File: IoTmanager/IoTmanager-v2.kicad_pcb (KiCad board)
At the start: 2 copper layers, 50 x 70.7 mm, 65 parts, among them J2 Conn_01x12_Pin, J3 Conn_01x12_Pin, J4-flash1 flash, J5 reset, K3 ZC32F-012-HS3-copy, K5 ZC32F-012-HS3-copy, K6 ZC32F-012-HS3-copy, K7 ZC32F-012-HS3-copy, Q1-pnp1 MMBT5401, Q10-pnp1 MMBT5401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

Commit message: update
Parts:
- removed U4: Mini360, module-custom-for-esp8266:Mini360_step-down
- added R12-10k2: R-1k, Resistor_SMD:R_0805_2012Metric, B.Cu at (107.7, 63.4)
- added R12-10k3: R-1k, Resistor_SMD:R_0805_2012Metric, B.Cu at (107.7, 66.3)
- added U3: DHT11, Sensor:Aosong_DHT11_5.5x12.0_P2.54mm, F.Cu at (122.6, 127.3)
- moved U5 52.1 mm to (127.0, 109.0), turned to 180 degrees
- moved R21 51.9 mm to (114.0, 126.0), turned to 0 degrees
- moved U3-tsop23 51.5 mm to (121.2, 85.9), turned to 90 degrees
- moved R25 51.3 mm to (82.8, 125.5), turned to 180 degrees
- moved Q10-pnp1 47.3 mm to (82.7, 122.8), turned to 0 degrees
- moved D1 47.2 mm to (122.2, 89.2), turned to -90 degrees
- moved Q5 46.5 mm to (113.7, 122.8), turned to 0 degrees
- moved R26 43.3 mm to (82.8, 120.0), turned to 180 degrees
- moved K3 43.0 mm to (119.0, 111.6), turned to -90 degrees
- moved R22 42.9 mm to (113.9, 120.1), turned to 0 degrees
- moved R4 42.6 mm to (103.7, 125.8), turned to 0 degrees
- moved R23 42.4 mm to (92.9, 125.6), turned to 0 degrees
- moved J2 41.8 mm to (80.0, 130.7), turned to 180 degrees
- moved D6 39.7 mm to (122.4, 112.4), turned to -90 degrees
- moved Q11-npn1 39.7 mm to (82.7, 117.1), turned to 0 degrees
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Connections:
- J2 pad 9: /d0 -> unconnected-(J2-Pin_9-Pad9)
- Jumper-d5 pad 1: /d5 -> Net-(IRLR2-G)
- Jumper-d6 pad 1: /d6 -> Net-(IRLR1-G)
- Jumper-d7 pad 1: /d7 -> Net-(IRLR3-G)
- U2 pad 19: /d2 -> Net-(U2-GPIO4)
- U2 pad 20: /d1 -> Net-(U2-GPIO5)
- U3-tsop23 pad 1: /d5 -> /d1
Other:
- board size 50 x 70.7 mm -> 48 x 80 mm

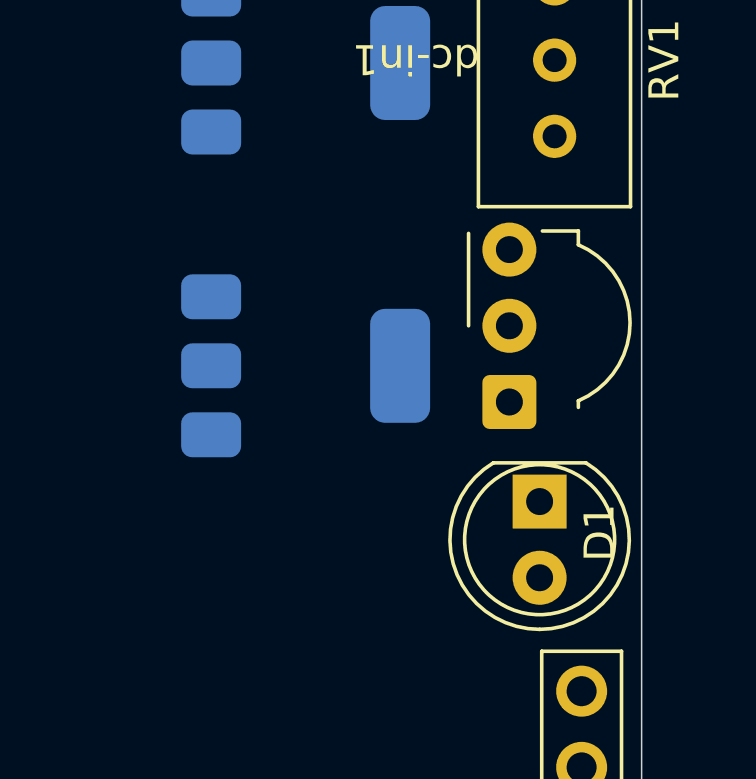
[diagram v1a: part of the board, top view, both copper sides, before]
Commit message: Update IoTmanager schematic and libraries
- Changed paper size from A3 to A2 in IoTmanager schematic.
- Added MMDT4413-7-F symbol and footprint to the schematic and libraries.
- Updated various component properties including reference, value, and footprint.
- Adjusted component placements and added new power symbols for +3.3V and GNDPWR.
- Modified existing project files in Proteous tests, including autosaved versions.
- Updated fp-info-cache with new component details.
- Created new KiCAD symbol and footprint files for MMDT4413-7-F.
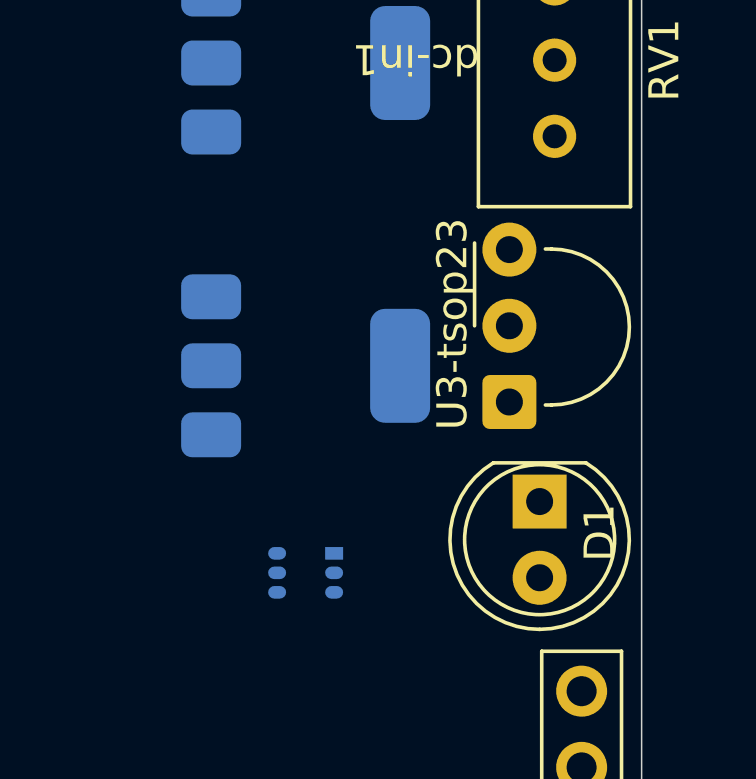
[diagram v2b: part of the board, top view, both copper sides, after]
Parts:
- added U8: MMDT4413-7-F, module-custom-for-esp8266:SOT-363_DIO, B.Cu at (114.4, 91.6)
- U3-tsop23: footprint OptoDevice:Vishay_MOLD-3Pin -> module-custom-for-esp8266:Vishay_MINIMOLD-3Pin_GND_correct
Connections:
- Q5 pad 1: Net-(Q5-B) -> unconnected-(Q5-B-Pad1)
- R21 pad 1: Net-(Q5-B) -> Net-(U8-B2)

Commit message: auto update from EPAM computer
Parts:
- added C3: C_Small, Capacitor_SMD:C_0805_2012Metric_Pad1.18x1.45mm_HandSolder, B.Cu at (117.0, 79.7)
- added R11: R-100, Resistor_SMD:R_0805_2012Metric, B.Cu at (116.5, 90.2)
- moved U8 3.37 mm to (114.0, 94.9)
- moved R7 0.40 mm to (119.5, 120.8)
- moved U3 0.13 mm to (122.7, 127.2)
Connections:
- R16 pad 2: /d8 -> /d2
- U3-tsop23 pad 1: /d1 -> Net-(U3-tsop23-OUT)

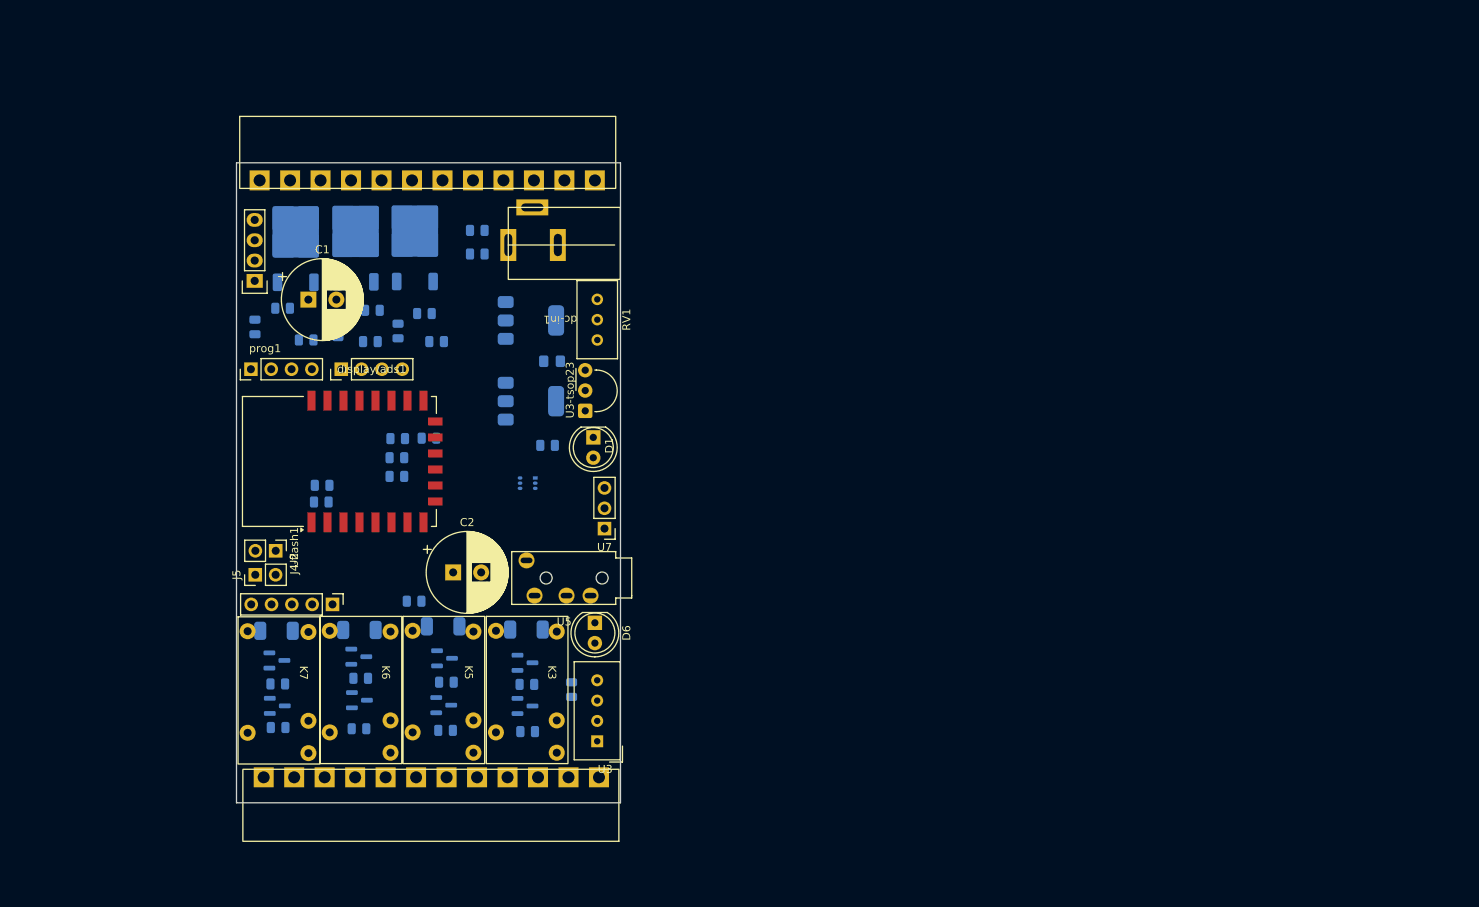
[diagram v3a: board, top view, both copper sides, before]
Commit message: Update fp-info-cache with new audio module and relay specifications
- Updated the ID for the Audio_Module entry.
- Added new relay module (RELAY_SRD-05VDC-SL-C) with specifications.
- Ensured proper formatting and consistency in the module entries.
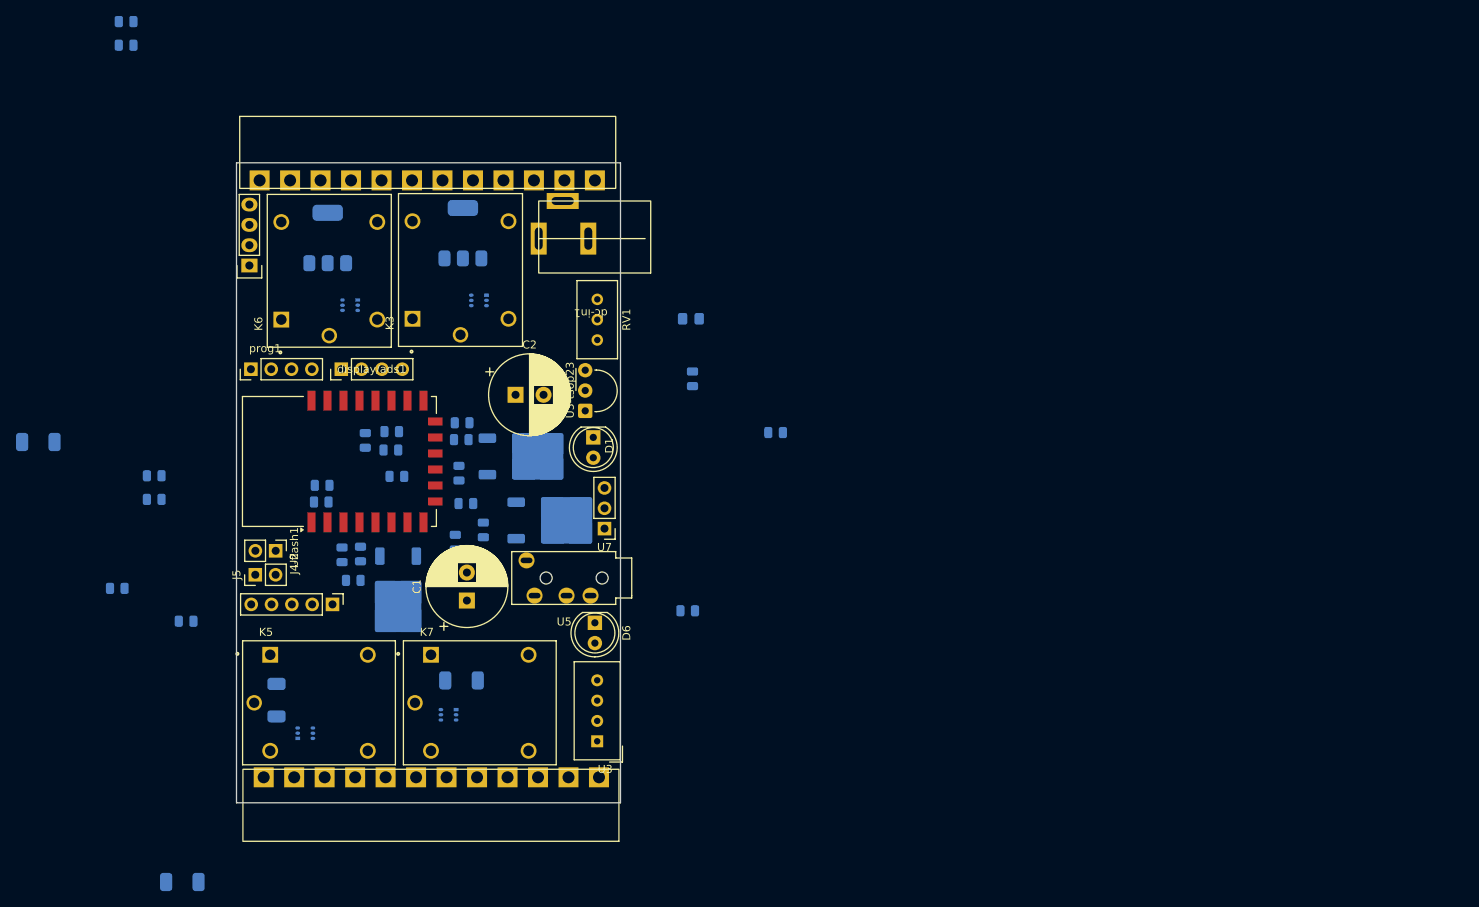
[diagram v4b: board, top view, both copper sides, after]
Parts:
- removed Q1-pnp1, Q10-pnp1, Q5, Q8-pnp1: MMBT5401, Package_TO_SOT_SMD:SOT-23
- removed Q11-npn1, Q6, Q7-npn1, Q9: MMBT5551-npn, Package_TO_SOT_SMD:SOT-23
- removed R17, R22, R23, R24, R25, R26: R-1k, Resistor_SMD:R_0805_2012Metric
- added R12: R-1k, Resistor_SMD:R_0805_2012Metric, B.Cu at (67.3, 94.0)
- added R14: R-1k, Resistor_SMD:R_0805_2012Metric, B.Cu at (67.3, 97.0)
- added U10: MMDT4413-7-F, module-custom-for-esp8266:SOT-363_DIO, B.Cu at (91.8, 72.7)
- added U11: MMDT4413-7-F, module-custom-for-esp8266:SOT-363_DIO, B.Cu at (104.1, 123.9)
- added U9: MMDT4413-7-F, module-custom-for-esp8266:SOT-363_DIO, B.Cu at (86.2, 126.2)
- K3, K5, K6, K7: footprint module-custom-for-esp8266:HF32F-005-ZS3 -> module-custom-for-esp8266:RELAY_SRD-05VDC-SL-C
- moved R21 54.3 mm to (62.7, 108.1)
- moved D2 53.3 mm to (72.1, 144.8)
- moved R12-10k2 51.1 mm to (63.8, 37.2)
- moved R12-10k3 51.1 mm to (63.8, 40.2)
- moved D4 46.5 mm to (54.1, 89.8)
- moved IRLR3 46.1 mm to (97.8, 109.1), turned to -90 degrees
- moved K3 45.3 mm to (105.6, 68.3), turned to 90 degrees
- moved K6 44.1 mm to (89.2, 68.4), turned to 90 degrees
- moved C1 42.5 mm to (106.4, 109.6), turned to 90 degrees
- moved R7 41.7 mm to (134.6, 81.9)
- moved IRLR2 39.1 mm to (117.6, 99.6), turned to 0 degrees
- moved R4 35.2 mm to (71.3, 112.2)
- moved IRLR1 34.4 mm to (114.0, 91.6), turned to 0 degrees
- moved R10 34.2 mm to (134.0, 110.9)
- moved Jumper-d7 34.0 mm to (92.2, 107.1), turned to 0 degrees
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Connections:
- R4 pad 2: /tx -> /d0
- U8 pad 6: unconnected-(U8-C1-Pad6) -> Net-(D2-A)

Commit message: auto update from EPAM computer
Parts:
- removed D6: LED, LED_THT:LED_D5.0mm
- removed MX-RM-5V-RF-sensor1: Conn_01x04_Pin, module-custom-for-esp8266:RF_Receiver_433_MHz
- removed R10: R-150, Resistor_SMD:R_0805_2012Metric
- removed display/ads1: Conn_01x04_Pin, Connector_PinHeader_2.54mm:PinHeader_1x04_P2.54mm_Vertical
- removed max1: ~, Connector_PinHeader_2.54mm:PinHeader_1x05_P2.54mm_Vertical
- U2: moved to B.Cu
- moved R12-10k2 71.7 mm to (94.7, 101.9), turned to 0 degrees
- moved D2 70.0 mm to (84.1, 75.8), turned to 0 degrees
- moved R12-10k3 56.8 mm to (105.2, 79.1), turned to 0 degrees
- moved R4 50.7 mm to (103.3, 72.8), turned to 180 degrees
- moved D4 48.1 mm to (100.2, 75.8), turned to 0 degrees
- moved R14 43.1 mm to (105.1, 117.7), turned to 90 degrees
- moved R21 43.0 mm to (87.9, 73.3), turned to 180 degrees
- moved J4-flash1 42.9 mm to (114.3, 74.6)
- moved J5 42.9 mm to (111.8, 77.6)
- moved C2 41.8 mm to (70.8, 85.8)
- moved R7 38.2 mm to (102.8, 103.0)
- moved R12 34.6 mm to (88.0, 121.8), turned to 0 degrees
- moved prog1 34.2 mm to (112.1, 70.7), turned to 180 degrees
- moved R16 33.9 mm to (122.0, 98.2), turned to 180 degrees
- moved IRLR2 32.7 mm to (89.2, 115.8), turned to 180 degrees
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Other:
- board size 48 x 80 mm -> 48 x 75 mm

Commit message: auto update from EPAM computer
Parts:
- moved C1 108.2 mm to (184.9, 63.1)
- moved C3 102.5 mm to (221.3, 84.3)
- moved R3 102.5 mm to (217.7, 83.6)
- moved U5 102.5 mm to (230.8, 104.9)
- moved U7 102.5 mm to (218.8, 92.1)
- moved R11 102.5 mm to (219.4, 88.9)
- moved RV1 102.5 mm to (214.2, 83.5)
- moved R16 102.5 mm to (224.6, 98.1)
- moved C2 96.4 mm to (165.5, 67.8)
- moved R9 46.4 mm to (69.6, 88.6), turned to 180 degrees
- moved R8 44.6 mm to (69.2, 96.4), turned to 180 degrees
- moved R12 37.7 mm to (108.1, 89.8), turned to 90 degrees
- moved U9 36.0 mm to (107.4, 93.6), turned to 90 degrees
- moved U11 33.8 mm to (91.0, 90.8), turned to -90 degrees
- moved K7 33.2 mm to (85.4, 90.7), turned to 90 degrees
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
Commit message: update
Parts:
- added SW1: SW_PUSH_6mm_H4.3mm, module-custom-for-esp8266:SW_PUSH_6mm_H4.3mm, F.Cu at (115.3, 111.3)
- moved U5 79.8 mm to (151.2, 99.4)
- moved C3 64.5 mm to (156.8, 82.4)
- moved R11 64.5 mm to (154.9, 87.1)
- moved R16 64.5 mm to (160.1, 96.3)
- moved R3 64.5 mm to (153.2, 81.8)
- moved RV1 64.5 mm to (149.7, 81.6)
- moved U7 64.5 mm to (154.3, 90.2)
- moved R1 19.0 mm to (115.7, 92.1), turned to 90 degrees
- moved D3 13.7 mm to (112.5, 89.9), turned to 90 degrees
- moved Jumper-d5 12.3 mm to (109.0, 93.5), turned to 180 degrees
- moved R14 11.2 mm to (90.6, 83.0), turned to 90 degrees
- moved D5 11.2 mm to (93.1, 89.8), turned to 90 degrees
- moved U9 11.0 mm to (109.8, 82.9), turned to 180 degrees
- moved U11 8.57 mm to (87.3, 83.1), turned to 0 degrees
- moved R12 7.85 mm to (106.0, 82.2), turned to 180 degrees
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
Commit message: update
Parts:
- added G***: LOGO, LOGO, F.Cu at (91.9, 105.3)
- added G***: LOGO, LOGO, F.Cu at (112.2, 118.8)
- added G***: LOGO, LOGO, B.Cu at (88.3, 120.0)
- added R12-10k4: R-1k, Resistor_SMD:R_0805_2012Metric, B.Cu at (118.3, 85.3)
- added R12-10k5: R-1k, Resistor_SMD:R_0805_2012Metric, B.Cu at (118.4, 88.5)
- R12-10k2, R12-10k3: value R-1k -> R-4k7
- moved C1 101.0 mm to (99.9, 117.7)
- moved C2 97.1 mm to (82.1, 117.6)
- moved U7 50.1 mm to (105.0, 99.2), turned to 90 degrees
- moved R8 46.8 mm to (108.6, 121.7), turned to 0 degrees
- moved R9 45.9 mm to (105.1, 120.9), turned to -90 degrees
- moved R16 41.7 mm to (118.5, 99.8)
- moved C3 38.9 mm to (122.0, 99.7), turned to 90 degrees
- moved R11 37.2 mm to (118.4, 80.1)
- moved R3 34.6 mm to (120.2, 92.1), turned to 180 degrees
- moved RV1 27.7 mm to (122.7, 87.8), turned to 90 degrees
- moved U5 23.9 mm to (127.6, 103.3)
- moved R2 10.7 mm to (97.1, 92.7), turned to 0 degrees
- moved U2 2.72 mm to (89.7, 107.0)
- moved SW1 2.47 mm to (117.8, 110.8)
- moved U3 0.75 mm to (122.5, 120.4)
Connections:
- J2 pad 12: /d8 -> Net-(J2-Pin_12)
- J2 pad 9: unconnected-(J2-Pin_9-Pad9) -> Net-(J2-Pin_9)
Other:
- board text added: "GND GND 12V 5V 3.3V D5 D6 D7 TX D1 D2 D8"
- board text added: "d3(0) tx d0(16) rx NC COM NO | NC COM NO | NC COM NO | NC COM NO"
